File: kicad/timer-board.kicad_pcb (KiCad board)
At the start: 2 copper layers, 61 x 27.9 mm, 18 parts, among them J1 Conn_PWR, J2 Conn_Data, SW1 SW_SPST, SW2 SW_SPDT, U1 NE555DR, U2 SN74HC00DR

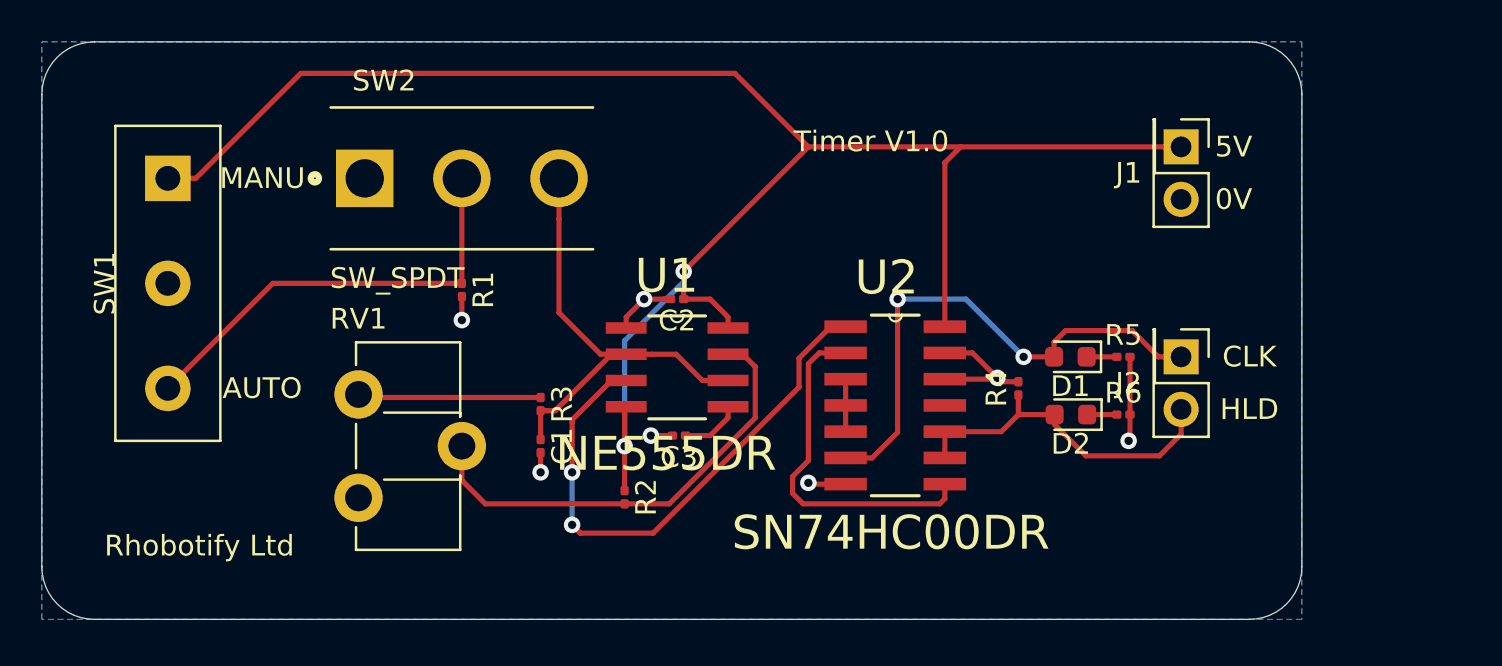
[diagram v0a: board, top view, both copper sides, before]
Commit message: Add holes
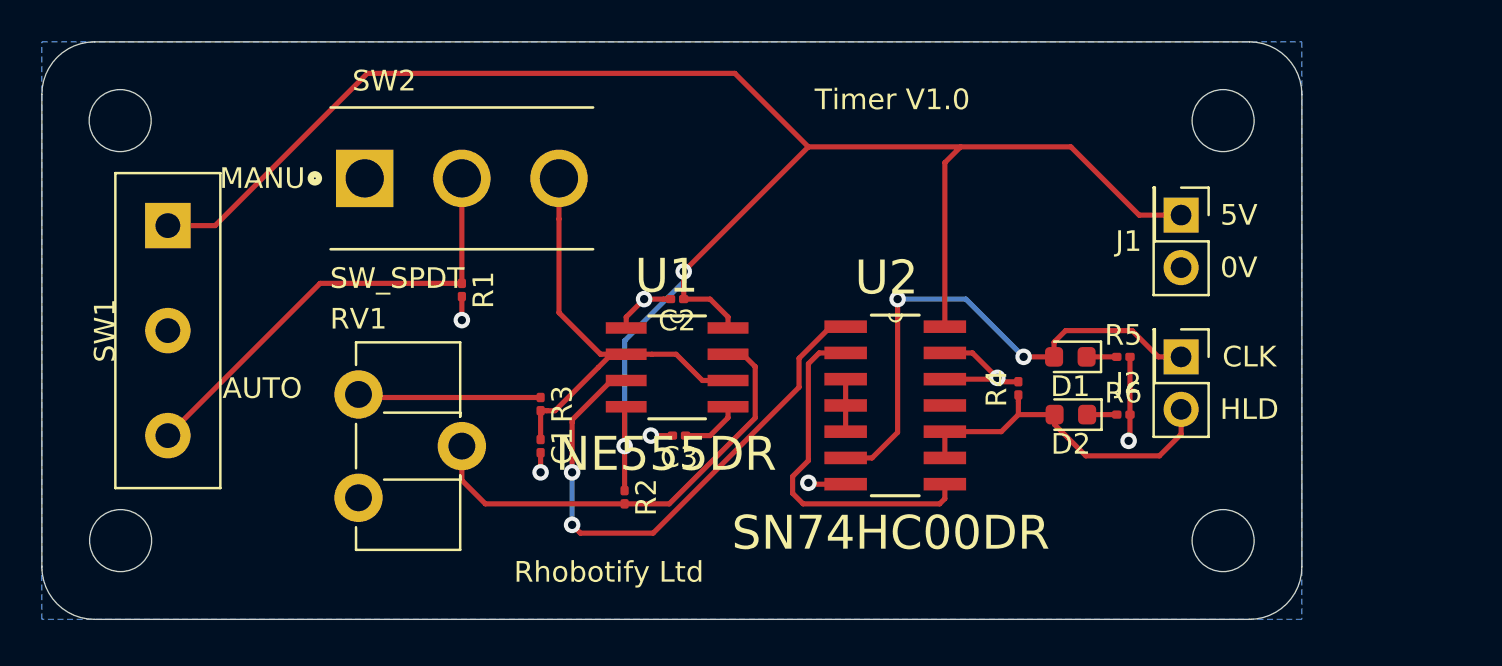
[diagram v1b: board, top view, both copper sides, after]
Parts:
- moved J1 3.30 mm to (359.9, 110.0)
- moved SW1 2.29 mm to (308.4, 115.6)
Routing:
- net +5V: track 88.2 -> 90.5 mm
- net Net-(R1-Pad1): track 21.4 -> 22.4 mm
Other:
- outline, holes or cut-outs redrawn
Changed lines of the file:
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@@
   (general
     (thickness 1.6)
-    (drawings 16)
-    (tracks 128)
+    (drawings 20)
+    (tracks 130)
     (zones 0)
     (modules 18)
@@
   )
   (module "mine:snap spst switch" (layer F.Cu)
-    (at 308.356 113.284 270)
+    (at 308.356 115.57 270)
     (fp_text reference SW1 (at 0 0.5 270) (layer F.SilkS)
       (effects (font (size 1 1) (thickness 0.15)))
@@
   )
   (module Connector_PinHeader_2.54mm:PinHeader_2x01_P2.54mm_Vertical (layer F.Cu)
-    (at 359.918 106.68 270)
+    (at 359.918 109.982 270)
     (descr "Through hole straight pin header, 2x01, 2.54mm pitch, double rows")
     (tags "Through hole pin header THT 2x01 2.54mm double row")
@@
       (net 10 +5V))
   )
+  (gr_circle (center 361.95 105.41) (end 363.45 105.41) (layer Edge.Cuts) (width 0.05))
+  (gr_circle (center 361.95 125.73) (end 363.45 125.73) (layer Edge.Cuts) (width 0.05))
+  (gr_circle (center 308.61 125.73) (end 310.11 125.73) (layer Edge.Cuts) (width 0.05))
+  (gr_circle (center 308.588979 105.41) (end 310.088979 105.41) (layer Edge.Cuts) (width 0.05))
   (gr_arc (start 363.22 127) (end 363.22 129.54) (angle -90) (layer Edge.Cuts) (width 0.05))
   (gr_arc (start 307.34 127) (end 304.8 127) (angle -90) (layer Edge.Cuts) (width 0.05))
   (gr_arc (start 307.34 104.14) (end 307.34 101.6) (angle -90) (layer Edge.Cuts) (width 0.05))
   (gr_arc (start 363.22 104.14) (end 365.76 104.14) (angle -90) (layer Edge.Cuts) (width 0.05))
-  (gr_text "Rhobotify Ltd" (at 312.42 125.984) (layer F.SilkS)
+  (gr_text "Rhobotify Ltd" (at 332.232 127.254) (layer F.SilkS)
     (effects (font (size 1 1) (thickness 0.15)))
   )
-  (gr_text "Timer V1.0" (at 344.932 106.426) (layer F.SilkS)
+  (gr_text "Timer V1.0" (at 345.948 104.394) (layer F.SilkS)
     (effects (font (size 1 1) (thickness 0.15)))
   )
@@
     (effects (font (size 1 1) (thickness 0.15)))
   )
-  (gr_text 0V (at 362.458 109.22) (layer F.SilkS)
+  (gr_text 0V (at 362.712 112.522) (layer F.SilkS)
     (effects (font (size 1 1) (thickness 0.15)))
   )
-  (gr_text 5V (at 362.458 106.68) (layer F.SilkS)
+  (gr_text 5V (at 362.712 109.982) (layer F.SilkS)
     (effects (font (size 1 1) (thickness 0.15)))
   )
@@
   (segment (start 355.346 116.84) (end 356.804 116.84) (width 0.25) (layer F.Cu) (net 5))
   (segment (start 325.12 113.284) (end 325.12 108.204) (width 0.25) (layer F.Cu) (net 6))
-  (segment (start 315.976 113.284) (end 310.896 118.364) (width 0.25) (layer F.Cu) (net 6))
-  (segment (start 325.12 113.284) (end 315.976 113.284) (width 0.25) (layer F.Cu) (net 6))
+  (segment (start 318.262 113.284) (end 310.896 120.65) (width 0.25) (layer F.Cu) (net 6))
+  (segment (start 325.12 113.284) (end 318.262 113.284) (width 0.25) (layer F.Cu) (net 6))
   (segment (start 325.12 122.812629) (end 325.12 121.158) (width 0.25) (layer F.Cu) (net 7))
   (segment (start 332.994 123.952) (end 326.259371 123.952) (width 0.25) (layer F.Cu) (net 7))
@@
   (segment (start 330.454 124.968) (end 330.853999 125.367999) (width 0.25) (layer F.Cu) (net 9))
   (segment (start 348.488 107.442) (end 348.488 115.38) (width 0.25) (layer F.Cu) (net 10))
-  (segment (start 359.918 106.68) (end 349.25 106.68) (width 0.25) (layer F.Cu) (net 10))
   (segment (start 349.25 106.68) (end 348.488 107.442) (width 0.25) (layer F.Cu) (net 10))
   (segment (start 341.884 106.68) (end 336.042 112.522) (width 0.25) (layer F.Cu) (net 10))
@@
   (segment (start 337.1302 114.046) (end 337.9978 114.9136) (width 0.25) (layer F.Cu) (net 10))
   (segment (start 335.854 114.046) (end 337.1302 114.046) (width 0.25) (layer F.Cu) (net 10))
-  (segment (start 341.884 106.68) (end 338.328 103.124) (width 0.25) (layer F.Cu) (net 10))
-  (segment (start 312.246 108.204) (end 310.896 108.204) (width 0.25) (layer F.Cu) (net 10))
-  (segment (start 317.326 103.124) (end 312.246 108.204) (width 0.25) (layer F.Cu) (net 10))
-  (segment (start 338.328 103.124) (end 317.326 103.124) (width 0.25) (layer F.Cu) (net 10))
   (segment (start 332.994 119.3292) (end 333.0702 119.253) (width 0.25) (layer F.Cu) (net 10))
   (via (at 332.994 121.158) (size 0.8) (drill 0.4) (layers F.Cu B.Cu) (net 10))
@@
   (segment (start 332.994 116.062802) (end 335.854 113.202802) (width 0.25) (layer B.Cu) (net 10))
   (segment (start 332.994 121.158) (end 332.994 116.062802) (width 0.25) (layer B.Cu) (net 10))
+  (segment (start 338.328 103.124) (end 320.548 103.124) (width 0.25) (layer F.Cu) (net 10))
+  (segment (start 341.884 106.68) (end 338.328 103.124) (width 0.25) (layer F.Cu) (net 10))
+  (segment (start 313.182 110.49) (end 310.896 110.49) (width 0.25) (layer F.Cu) (net 10))
+  (segment (start 320.548 103.124) (end 313.182 110.49) (width 0.25) (layer F.Cu) (net 10))
+  (segment (start 349.25 106.68) (end 354.584 106.68) (width 0.25) (layer F.Cu) (net 10))
+  (segment (start 357.886 109.982) (end 359.918 109.982) (width 0.25) (layer F.Cu) (net 10))
+  (segment (start 354.584 106.68) (end 357.886 109.982) (width 0.25) (layer F.Cu) (net 10))
   (segment (start 353.7965 119.634) (end 353.7965 120.1165) (width 0.25) (layer F.Cu) (net 11))
   (segment (start 359.918 120.582081) (end 359.918 119.38) (width 0.25) (layer F.Cu) (net 11))

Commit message: Thicken VCC
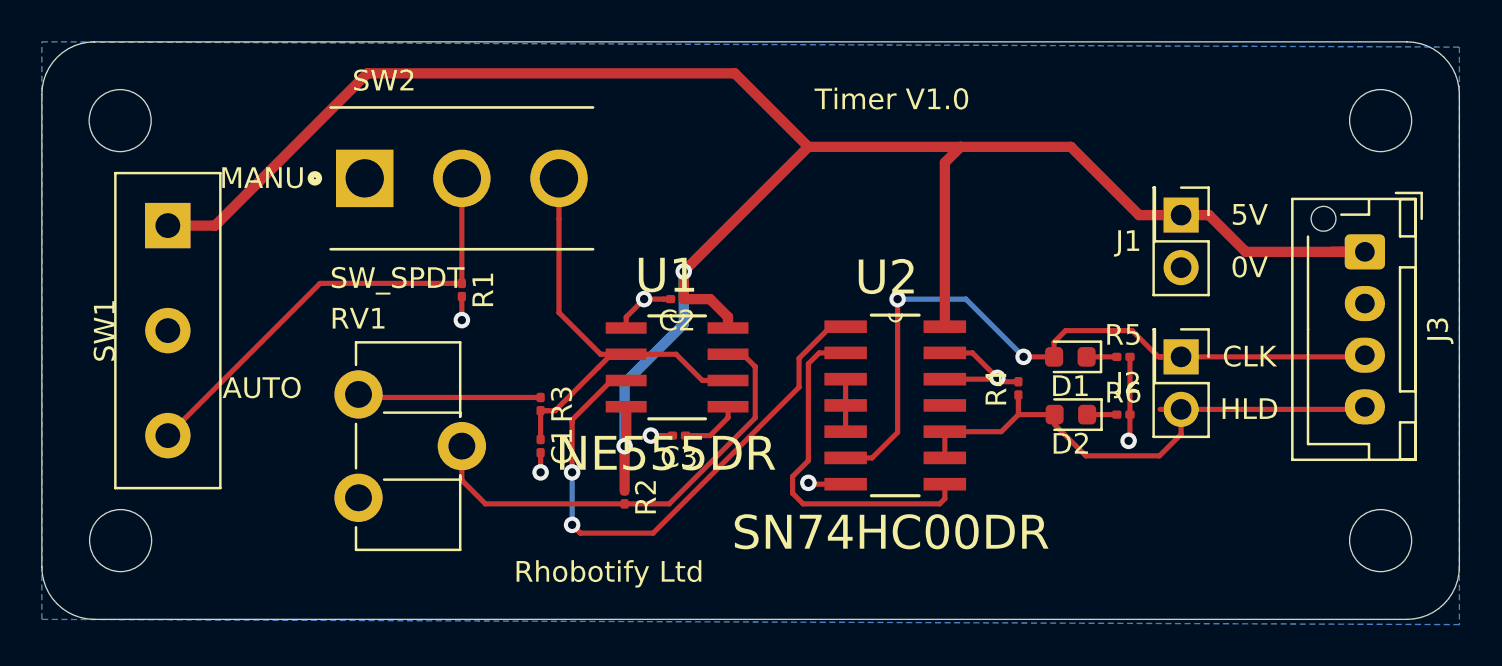
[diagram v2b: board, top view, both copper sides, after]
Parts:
- added J3: JST Conn, Connector_JST:JST_XH_B4B-XH-AM_1x04_P2.50mm_Vertical, F.Cu at (368.8, 111.8)
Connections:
- net Net-(D1-Pad2) renamed /Clk
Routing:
- net +5V: track 90.5 -> 100.8 mm
- net /Hold: track 16.7 -> 26.7 mm
- net /Clk: track 26.5 -> 36.5 mm
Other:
- board size 61 x 27.9 mm -> 68.6 x 27.9 mm
